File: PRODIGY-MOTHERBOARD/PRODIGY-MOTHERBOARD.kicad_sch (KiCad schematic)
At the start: 0 parts

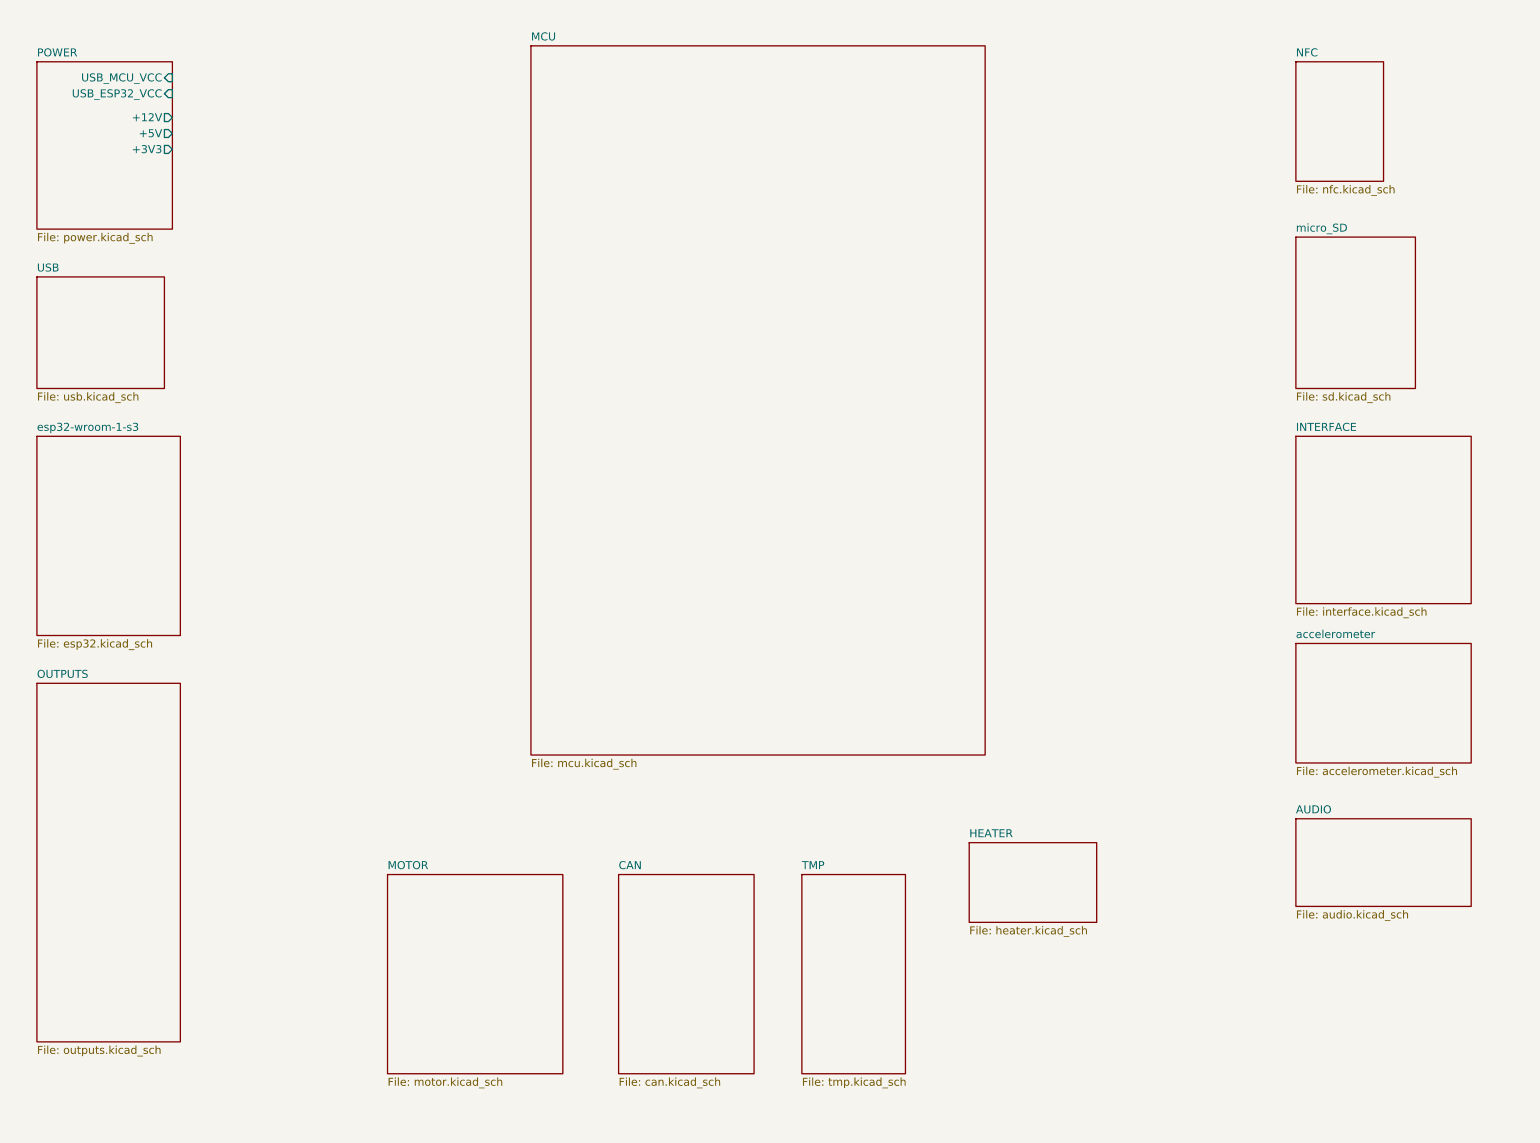
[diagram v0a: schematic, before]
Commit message: project restructure done. Hierarchical sheet done. Outputs/breakouts sheet done
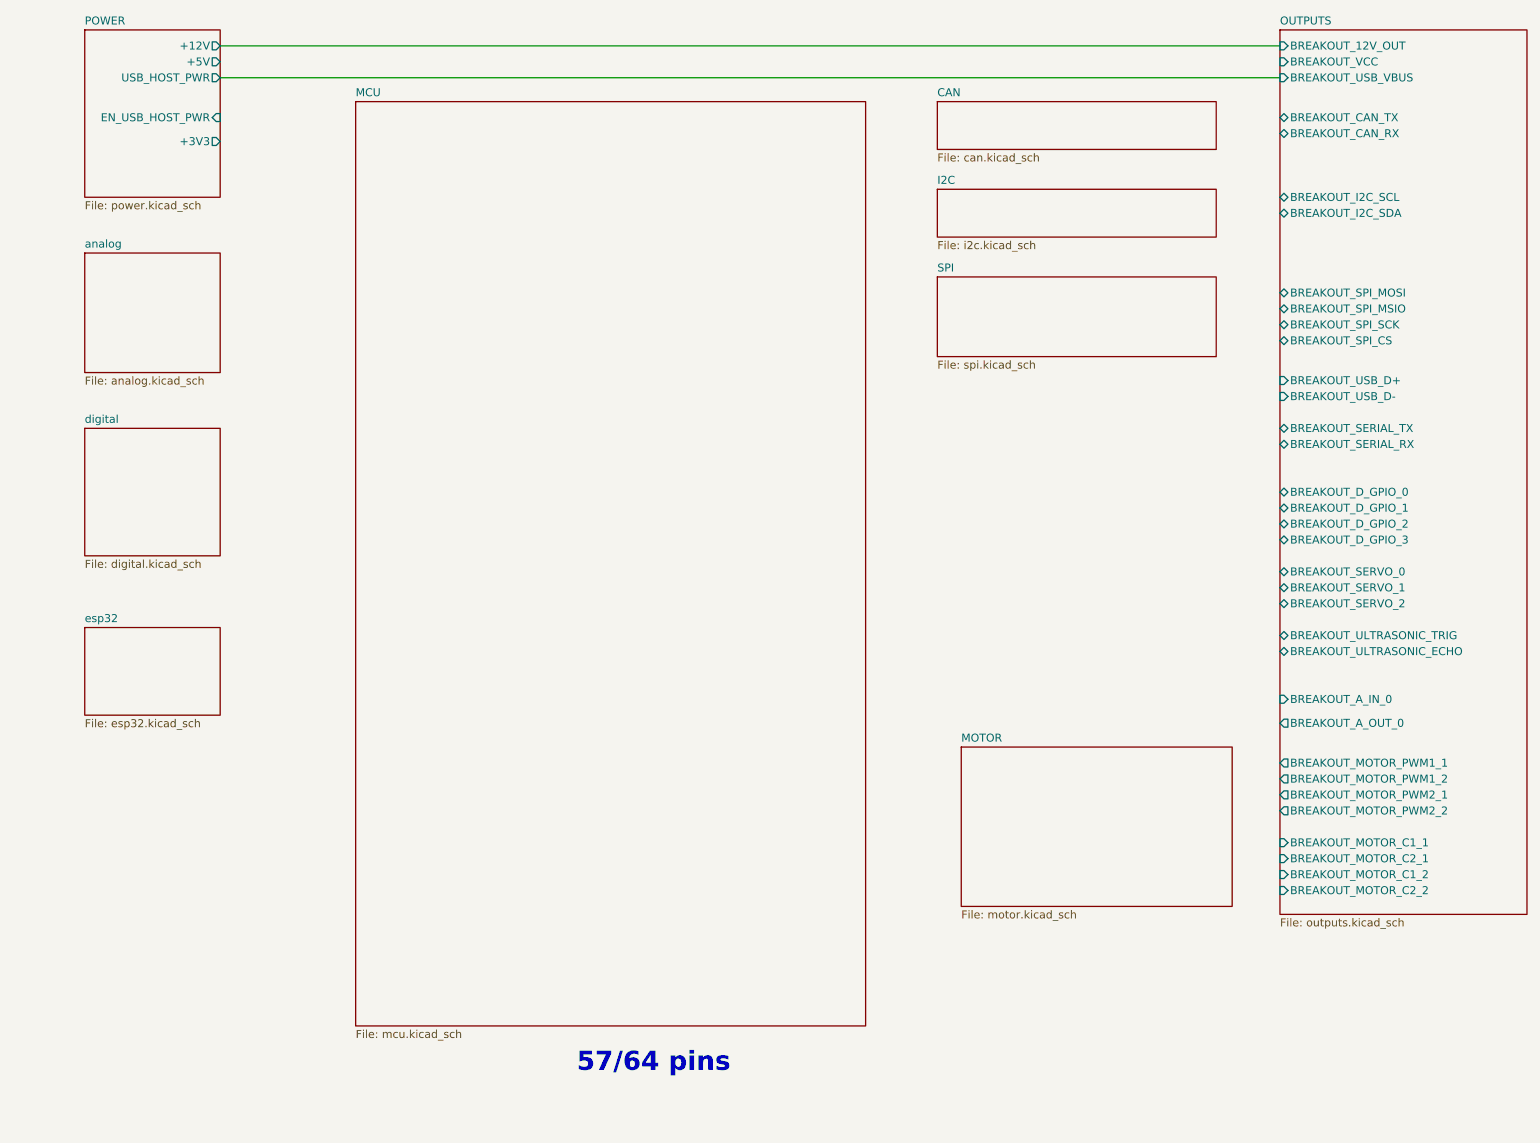
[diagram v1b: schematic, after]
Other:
- removed sheet AUDIO
- removed sheet HEATER
- removed sheet INTERFACE
- removed sheet NFC
- removed sheet TMP
- removed sheet USB
- removed sheet accelerometer
- removed sheet esp32-wroom-1-s3
- removed sheet micro_SD
- added sheet I2C (i2c.kicad_sch)
- added sheet SPI (spi.kicad_sch)
- added sheet analog (analog.kicad_sch)
- added sheet digital (digital.kicad_sch)
- added sheet esp32 (esp32.kicad_sch)
- sheet OUTPUTS ports: added BREAKOUT_12V_OUT, BREAKOUT_A_IN_0, BREAKOUT_A_OUT_0, BREAKOUT_CAN_RX, BREAKOUT_CAN_TX, BREAKOUT_D_GPIO_0, BREAKOUT_D_GPIO_1, BREAKOUT_D_GPIO_2, BREAKOUT_D_GPIO_3, BREAKOUT_I2C_SCL, BREAKOUT_I2C_SDA, BREAKOUT_MOTOR_C1_1, BREAKOUT_MOTOR_C1_2, BREAKOUT_MOTOR_C2_1, BREAKOUT_MOTOR_C2_2, BREAKOUT_MOTOR_PWM1_1, BREAKOUT_MOTOR_PWM1_2, BREAKOUT_MOTOR_PWM2_1, BREAKOUT_MOTOR_PWM2_2, BREAKOUT_SERIAL_RX, BREAKOUT_SERIAL_TX, BREAKOUT_SERVO_0, BREAKOUT_SERVO_1, BREAKOUT_SERVO_2, BREAKOUT_SPI_CS, BREAKOUT_SPI_MOSI, BREAKOUT_SPI_MSIO, BREAKOUT_SPI_SCK, BREAKOUT_ULTRASONIC_ECHO, BREAKOUT_ULTRASONIC_TRIG, BREAKOUT_USB_D+, BREAKOUT_USB_D-, BREAKOUT_USB_VBUS, BREAKOUT_VCC; removed none
- sheet POWER ports: added EN_USB_HOST_PWR, USB_HOST_PWR; removed USB_ESP32_VCC, USB_MCU_VCC
- note added: "57/64 pins"

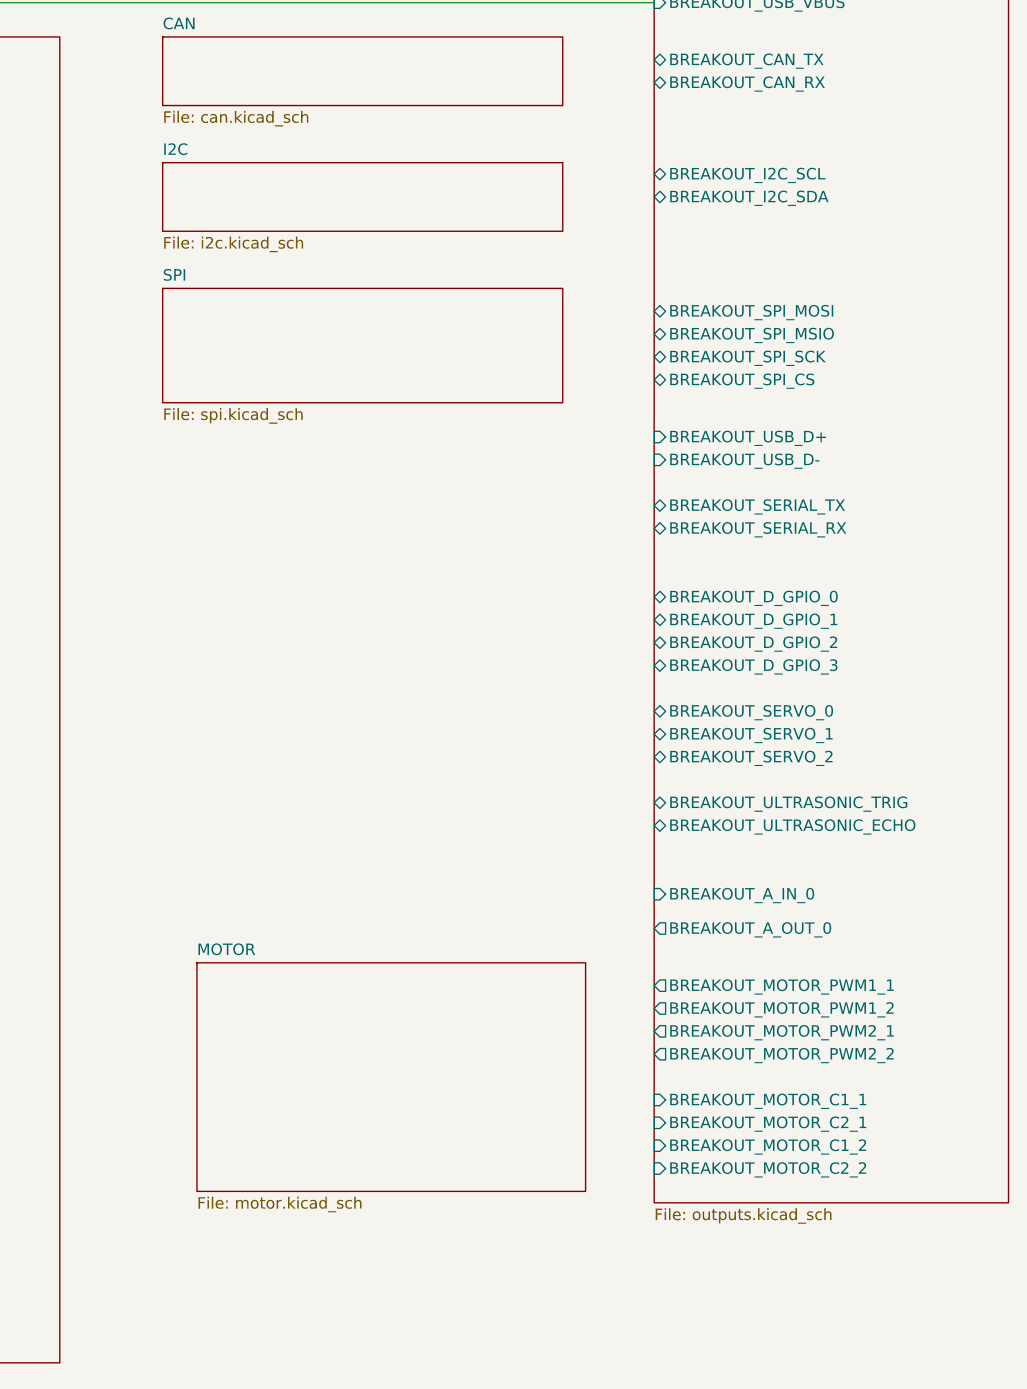
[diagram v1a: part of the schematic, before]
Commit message: Finished I2C device and bus schematics. Added logic level translation.
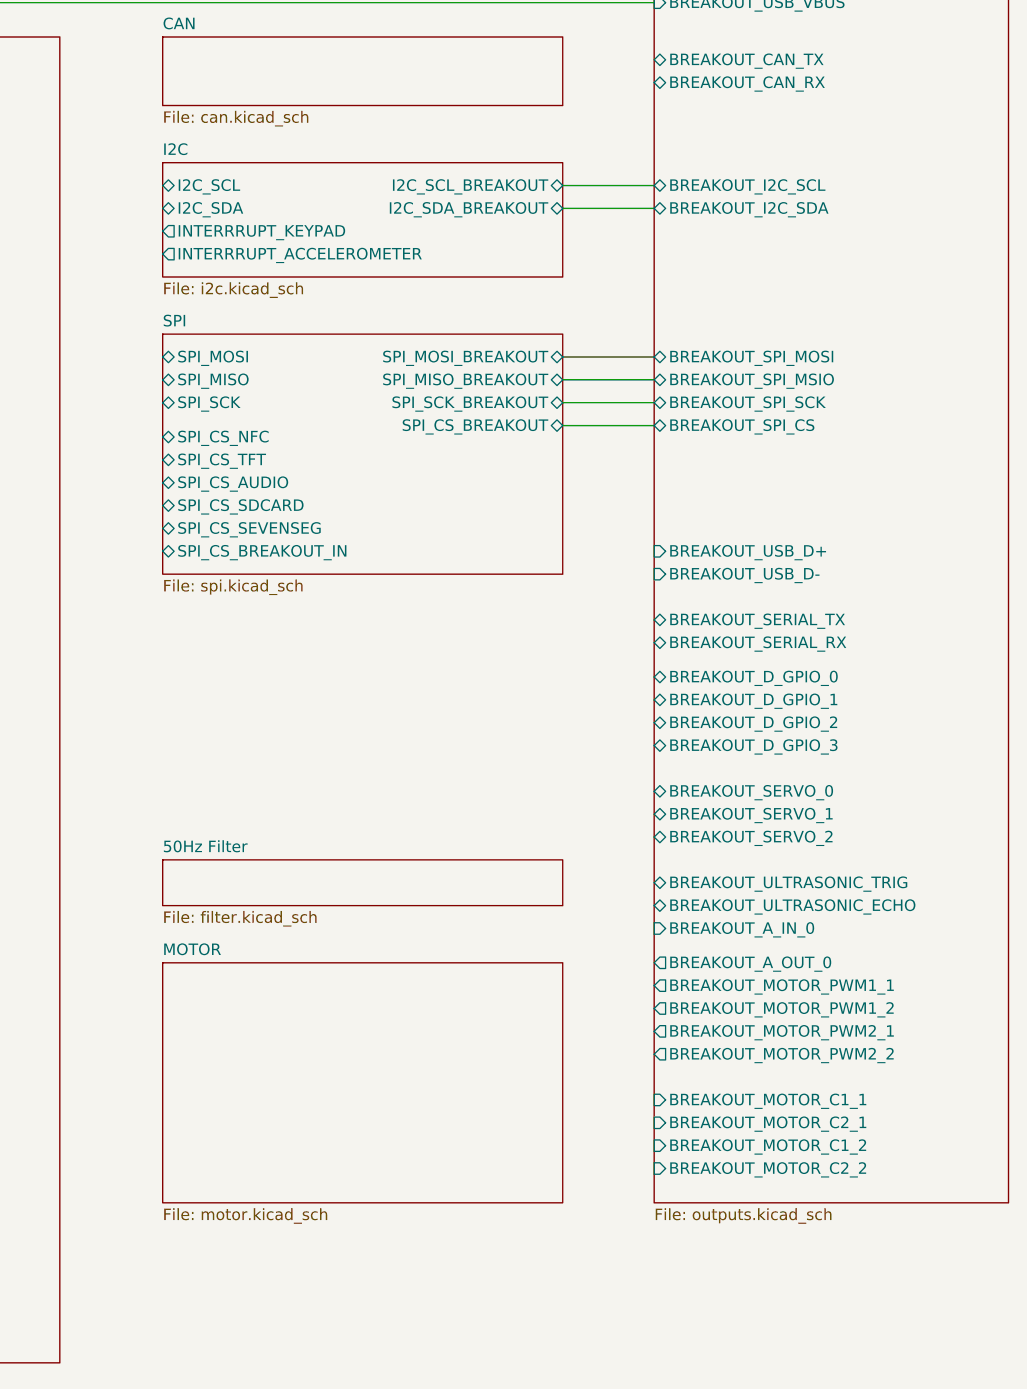
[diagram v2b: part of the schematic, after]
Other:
- added sheet 50Hz Filter (filter.kicad_sch)
- sheet I2C ports: added I2C_SCL, I2C_SCL_BREAKOUT, I2C_SDA, I2C_SDA_BREAKOUT, INTERRRUPT_ACCELEROMETER, INTERRRUPT_KEYPAD; removed none
- sheet SPI ports: added SPI_CS_AUDIO, SPI_CS_BREAKOUT, SPI_CS_BREAKOUT_IN, SPI_CS_NFC, SPI_CS_SDCARD, SPI_CS_SEVENSEG, SPI_CS_TFT, SPI_MISO, SPI_MISO_BREAKOUT, SPI_MOSI, SPI_MOSI_BREAKOUT, SPI_SCK, SPI_SCK_BREAKOUT; removed none

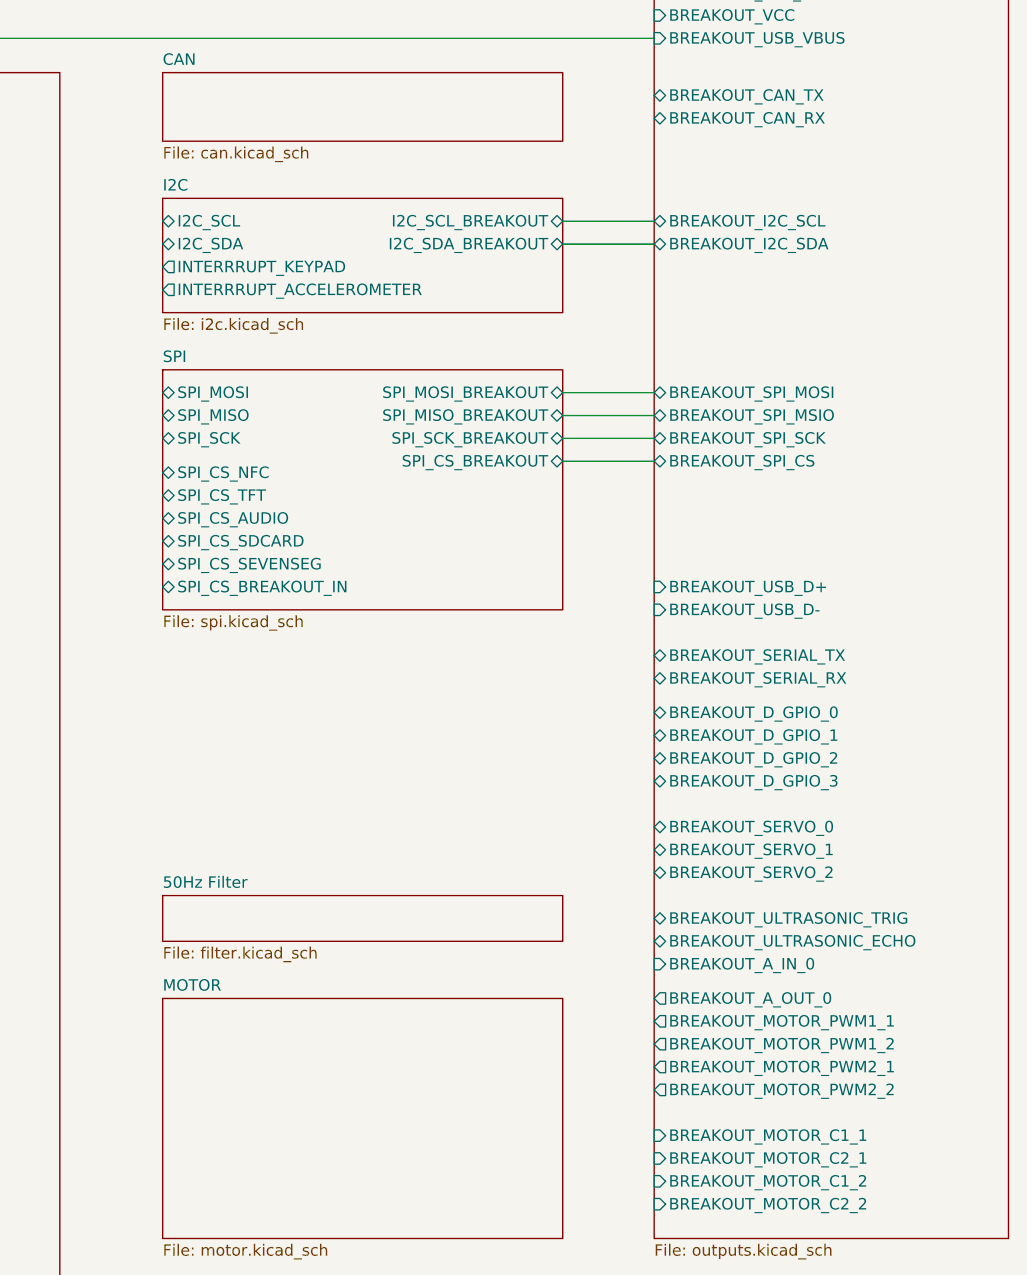
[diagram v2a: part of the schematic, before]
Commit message: SPI SD CARD circuit added.
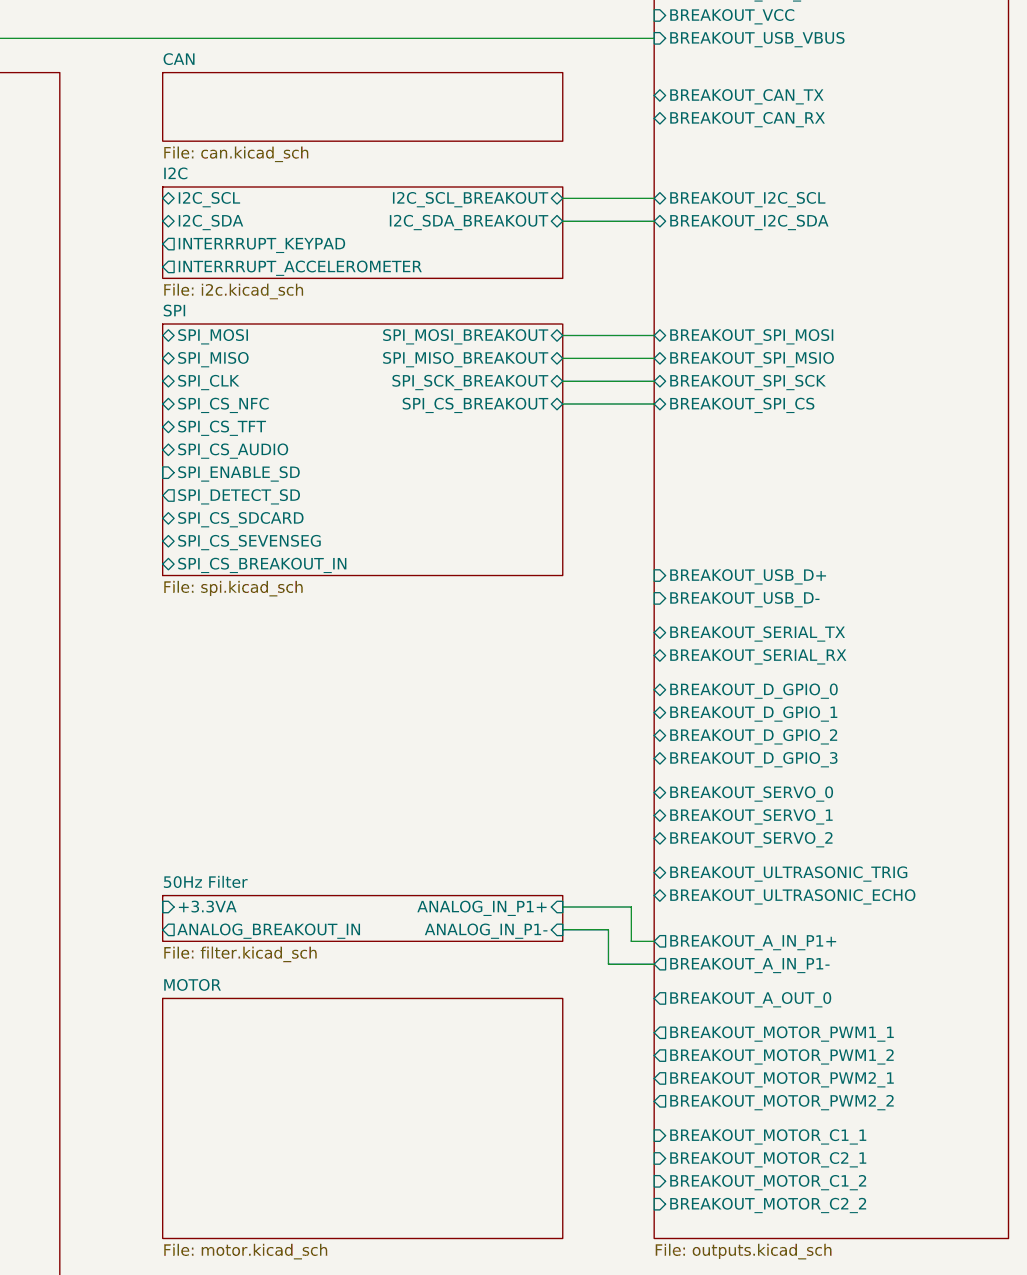
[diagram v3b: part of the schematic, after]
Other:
- sheet 50Hz Filter ports: added +3.3VA, ANALOG_BREAKOUT_IN, ANALOG_IN_P1+, ANALOG_IN_P1-; removed none
- sheet OUTPUTS ports: added BREAKOUT_A_IN_P1+, BREAKOUT_A_IN_P1-; removed BREAKOUT_A_IN_0
- sheet SPI ports: added SPI_CLK, SPI_DETECT_SD, SPI_ENABLE_SD; removed SPI_SCK
